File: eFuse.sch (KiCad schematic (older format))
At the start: 8 parts, among them U3 TPS25921x

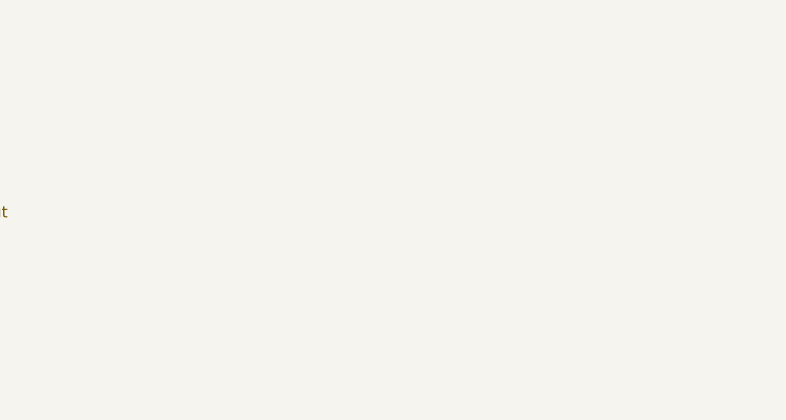
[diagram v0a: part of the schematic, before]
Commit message: Change Sheets to US Letter
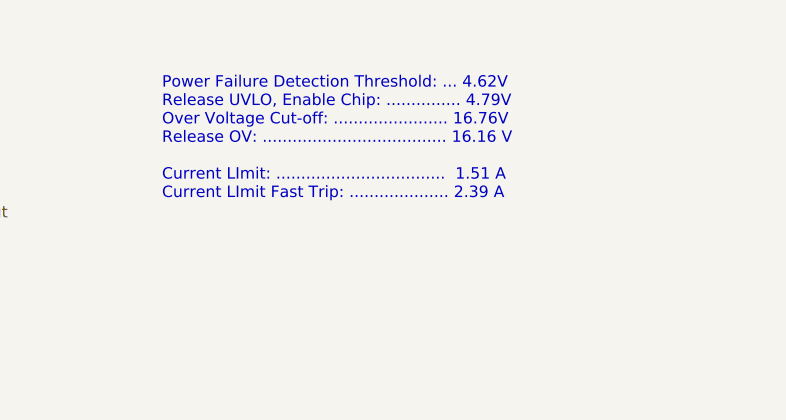
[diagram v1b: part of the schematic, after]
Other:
- note added: "Power Failure Detection Threshold: ... 4.62V\nRelease UVLO, Enable Chip: ............... 4.79V\nOver Voltage Cut-off: ....................... 16.76V\nRelease OV: ..................................... 16.16 V\n\nCurrent LImit: .................................. 1.51 A\nCurrent LImit Fast Trip: .................... 2.39 A"
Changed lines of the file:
@@
 EELAYER 30 0
 EELAYER END
-$Descr A4 11693 8268
+$Descr USLetter 11000 8500
 encoding utf-8
 Sheet 5 5
-Title ""
+Title "eFuse"
 Date "2020-10-17"
-Rev "2"
+Rev "3"
 Comp ""
 Comment1 ""
@@
 Wire Wire Line
 	6200 3150 6200 3050
+Text Notes 7450 2300 0    50   ~ 0
+Power Failure Detection Threshold: ... 4.62V\nRelease UVLO, Enable Chip: ............... 4.79V\nOver Voltage Cut-off: ....................... 16.76V\nRelease OV: ..................................... 16.16 V\n\nCurrent LImit: ..................................  1.51 A\nCurrent LImit Fast Trip: .................... 2.39 A
 $EndSCHEMATC
